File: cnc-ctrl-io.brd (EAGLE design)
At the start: 160 x 100 mm, 76 parts, among them IC1 MAX304SE, IC2 MAX304SE, IC8 MAX3072EESA, J2 22-05-7048-04, U1 TLC082D

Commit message: DDLMV1-Inputs hinzugefügt @work
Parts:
- added D10, D11, D12, D13, D14: (no value), diode:SMB
- added Q1, Q2, Q3, Q4, Q5: BCX71SMD, transistor-pnp:SOT23
- added R31, R32, R33, R34, R35, R37, R38: 4K7, rcl:R0603
- moved R13 20.2 mm to (132.3, 6.45), turned to 45 degrees
- moved OK6 18.4 mm to (136.5, 2.64), turned to 45 degrees
- moved C7 16.9 mm to (124.5, -42.9), turned to 90 degrees
- moved R9 16.5 mm to (128.0, 2.19), turned to 45 degrees
- moved R18 16.4 mm to (139.9, -2.53), turned to 135 degrees
- moved OK1 14.2 mm to (132.3, -1.63), turned to 45 degrees
- moved R10 13.4 mm to (123.7, -2.08), turned to 45 degrees
- moved R14 11.8 mm to (135.6, -6.79), turned to 135 degrees
- moved R11 11.4 mm to (119.5, -6.34), turned to 45 degrees
- moved R12 11.0 mm to (115.2, -10.6), turned to 45 degrees
- moved OK3 10.3 mm to (128.0, -5.89), turned to 45 degrees
- moved OK4 7.36 mm to (123.7, -10.2), turned to 45 degrees
- moved R15 7.27 mm to (131.4, -11.1), turned to 135 degrees
- moved OK5 6.67 mm to (119.5, -14.4), turned to 45 degrees
- moved J2 6.35 mm to (118.4, -41.0)
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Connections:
- new net COM@IN_1_3: MOD1.COM@IN_1_3, Q1.2, Q2.2, Q3.2, R34.2
- new net COM@IN_4_6: MOD1.COM@IN_4_6, Q4.2, Q5.2, R35.2
- new net N$21: MOD1.IN01, Q1.3
- new net N$28: MOD1.IN03, Q3.3
- new net N$29: MOD1.IN04, Q4.3
- new net N$30: Q3.1, R31.2
- new net N$31: Q2.1, R32.2
- new net N$32: Q1.1, R33.2
- new net N$33: MOD1.IN05, Q5.3
- new net N$36: Q5.1, R37.2
- new net N$37: Q4.1, R38.2
- new net N$40: R24.2
- net +5V: now also R34.1, R35.1
- net ESTOP: now also R38.1
- net ESTOP_IN: now also D11.C
- net N$27: now also MOD1.IN02, Q2.3; no longer MOD1.VOUT
- net PROBE: now also R31.1
- net PROBE_IN: now also D10.C
- net SGND: now also D10.A, D11.A, D12.A, D13.A, D14.A
- net SPINDLE_SPEED: now also MOD1.VOUT
- net X_END: now also R32.1
- net X_END_IN: now also D12.C
- net Y_END: now also R33.1
- net Y_END_IN: now also D13.C
- net Z_END: now also R37.1; no longer R24.2
- net Z_END_IN: now also D14.C

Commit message: Routing fertig @work
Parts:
- added R36: 4K7, rcl:R0603
- moved R25 120.6 mm to (137.0, -5.87), flipped to the bottom, turned to 0 degrees
- moved C6 118.8 mm to (135.3, -9.21), flipped to the bottom, turned to 0 degrees
- moved C5 116.7 mm to (137.0, -7.62), flipped to the bottom, turned to 180 degrees
- moved R27 115.5 mm to (142.4, -13.0), flipped to the bottom, turned to 270 degrees
- moved R26 115.4 mm to (142.4, -9.84), flipped to the bottom, turned to 270 degrees
- moved U1 114.9 mm to (136.7, -12.9), flipped to the bottom, turned to 270 degrees
- moved R13 75.3 mm to (59.8, -14.1), turned to 315 degrees
- moved R9 67.6 mm to (61.9, -12.1), turned to 315 degrees
- moved R10 61.2 mm to (63.2, -10.9), turned to 315 degrees
- moved R28 57.9 mm to (128.7, -8.73), flipped to the bottom, turned to 90 degrees
- moved R11 54.9 mm to (64.6, -9.45), turned to 315 degrees
- moved C12 54.2 mm to (83.5, -0.05), turned to 135 degrees
- moved R12 49.2 mm to (66.1, -8.04), turned to 315 degrees
- moved IC3 39.5 mm to (84.9, 9.53), turned to 0 degrees
- moved C11 38.9 mm to (79.9, 6.99)
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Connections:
- removed net +5V/1: JP2.3
- removed net N$19: OK10.2, R23.2
- removed net N$40: R24.2
- new net 12V: C6.2, C9.+, J1.A31, R30.1, U1.8
- net +12V: no longer C6.2, U1.8
- net +3V3: now also C20.1, IC8.2, IC8.3, IC8.8, R36.1
- net +5V: now also JP2.3
- net ENABLE1: now also R36.2
- net IF_PWR: no longer C20.1, IC8.8
- net N$1: now also OK9.2, R23.2; no longer C9.+, J1.A31, R30.1
- net N$18: now also OK10.2; no longer OK9.2
- net OUT_#1_A: now also J1.A27, OK10.3; no longer J1.A28, OK9.3
- net OUT_#1_B: now also J1.C27, OK10.4; no longer J1.C28, OK9.4
- net OUT_#2_A: now also J1.A28, OK9.3; no longer J1.A27, OK10.3
- net OUT_#2_B: now also J1.C28, OK9.4; no longer J1.C27, OK10.4
- net SGND: now also J1.A22, J1.A23, J1.A24, J1.A25, J1.A26
- net Z_END: now also R24.2
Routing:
- net PE: track 0.00 -> 405.4 mm
- net Z_END: track 0.00 -> 254.0 mm, vias 0 -> 5
- net ENABLE1: track 0.00 -> 236.9 mm, vias 0 -> 3
- net OUT_#2: track 0.00 -> 222.0 mm, vias 0 -> 1
- net OUT_#1: track 0.00 -> 218.1 mm, vias 0 -> 1
- net ESTOP: track 0.00 -> 214.7 mm, vias 0 -> 3
- net PROBE: track 0.00 -> 198.6 mm, vias 0 -> 3
- net X_END: track 0.00 -> 188.7 mm, vias 0 -> 3
- net Y_END: track 0.00 -> 174.6 mm, vias 0 -> 3
- net SPINDLE_ENABLE: track 0.00 -> 157.4 mm, vias 0 -> 3
- net SGND: track 0.00 -> 152.4 mm
- net SPINDLE_SPEED: track 0.00 -> 139.4 mm, vias 0 -> 1
- net SPINDLE: track 0.00 -> 126.1 mm, vias 0 -> 1
- net AGND: track 0.00 -> 121.3 mm, vias 0 -> 2
- net GND: track 0.00 -> 92.5 mm, vias 0 -> 7
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- added copper zone on layer 1, net +3V3
- added copper zone on layer 1, net +5V
- added copper zone on layer 16, net GND

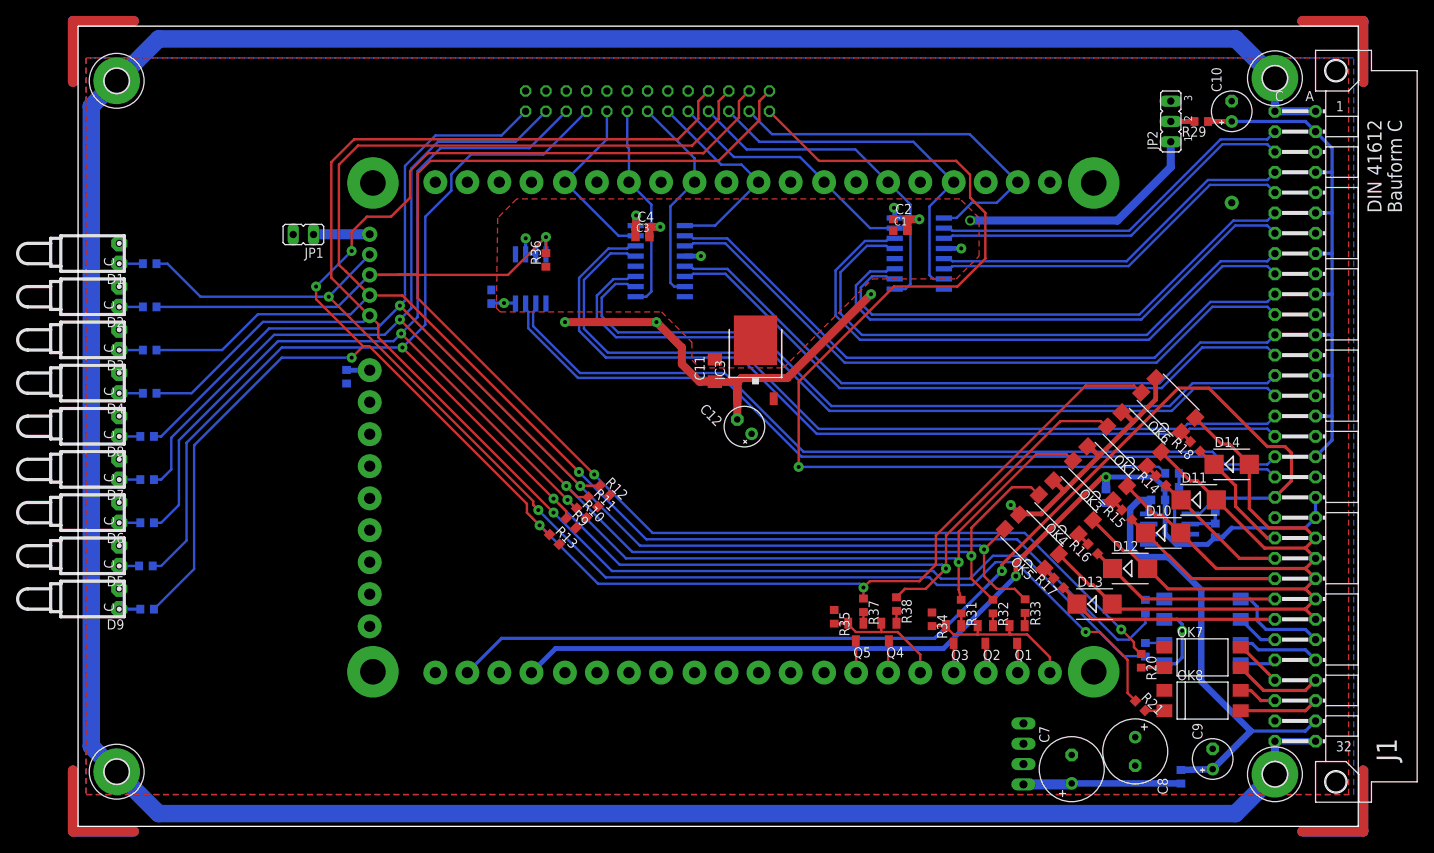
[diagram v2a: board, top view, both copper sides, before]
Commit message: lpt-connector verschoben, beschaltung für schirmung angepasst
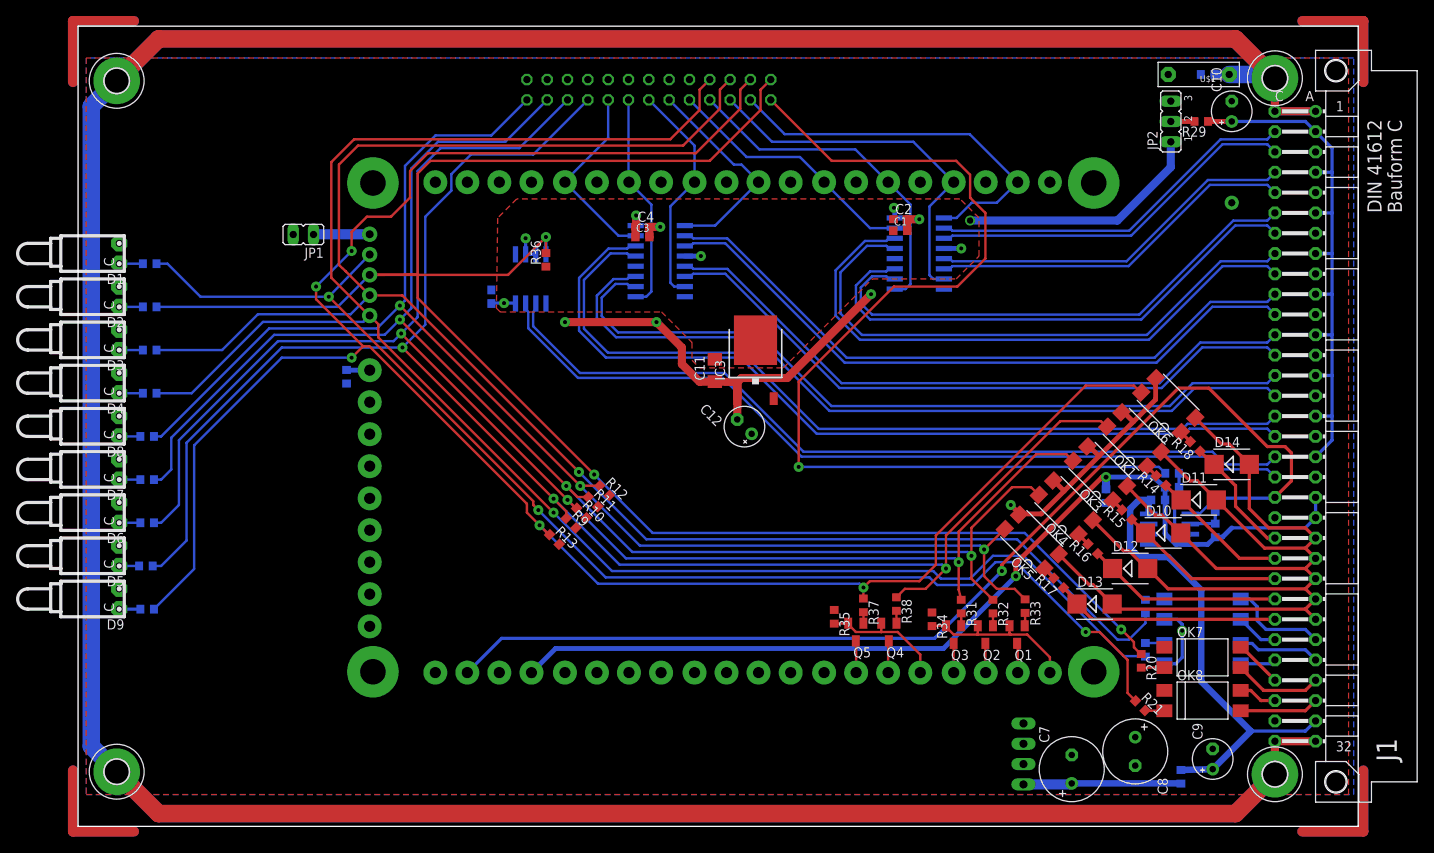
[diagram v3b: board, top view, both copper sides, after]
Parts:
- added R39: 1M, rcl:R0603
- added U$1: 0,01µF, Capacitor-Wima-MKS4-250v:R7K5B3
- moved SV1 1.44 mm to (71.6, 42.1)
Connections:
- net GND: now also R39.2, U$1.2
- net PE: now also R39.1, U$1.1
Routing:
- net PE: track 405.4 -> 729.5 mm
- net A_DIR: track 22.6 -> 24.1 mm
- net Z_DIR: track 27.1 -> 28.5 mm
- net A_STEP: track 26.0 -> 27.4 mm
- net Z_END: track 254.0 -> 254.9 mm
- net OUT_#2: track 222.0 -> 222.9 mm
- net OUT_#1: track 218.1 -> 219.0 mm
- net ENABLE1: track 236.9 -> 237.8 mm
- net Y_END: track 174.6 -> 175.3 mm
- net ESTOP: track 214.7 -> 215.4 mm
- net PROBE: track 198.6 -> 199.3 mm
- net X_END: track 188.7 -> 189.4 mm
